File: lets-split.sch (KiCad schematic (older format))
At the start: 54 parts

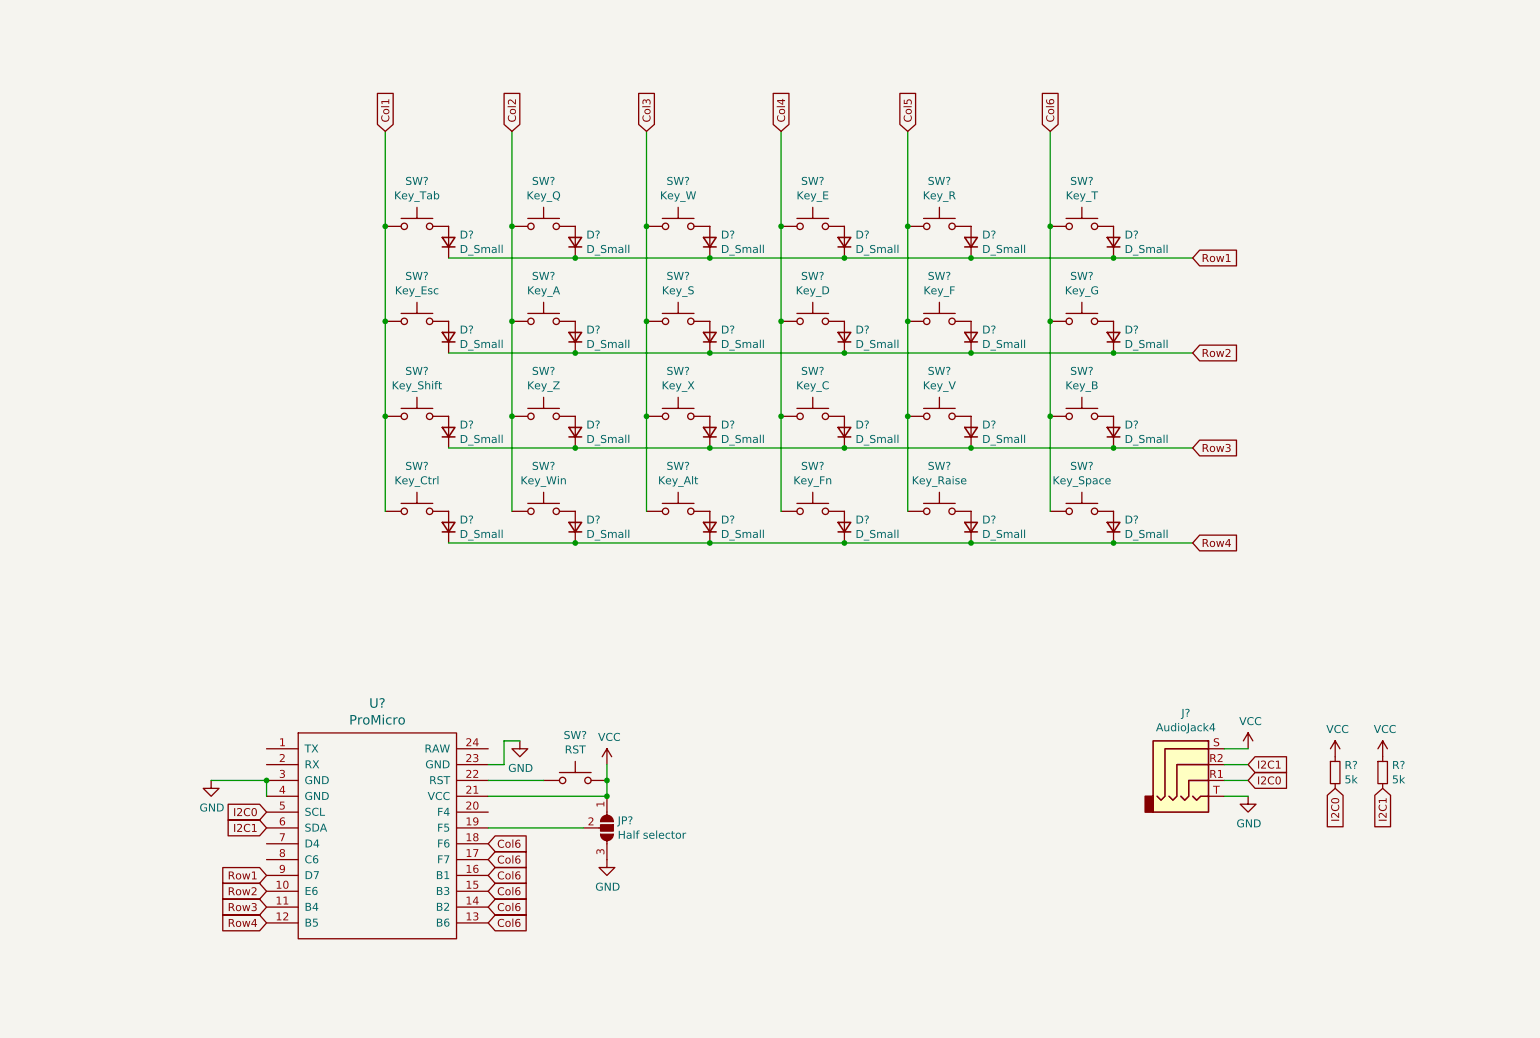
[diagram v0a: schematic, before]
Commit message: added annotations
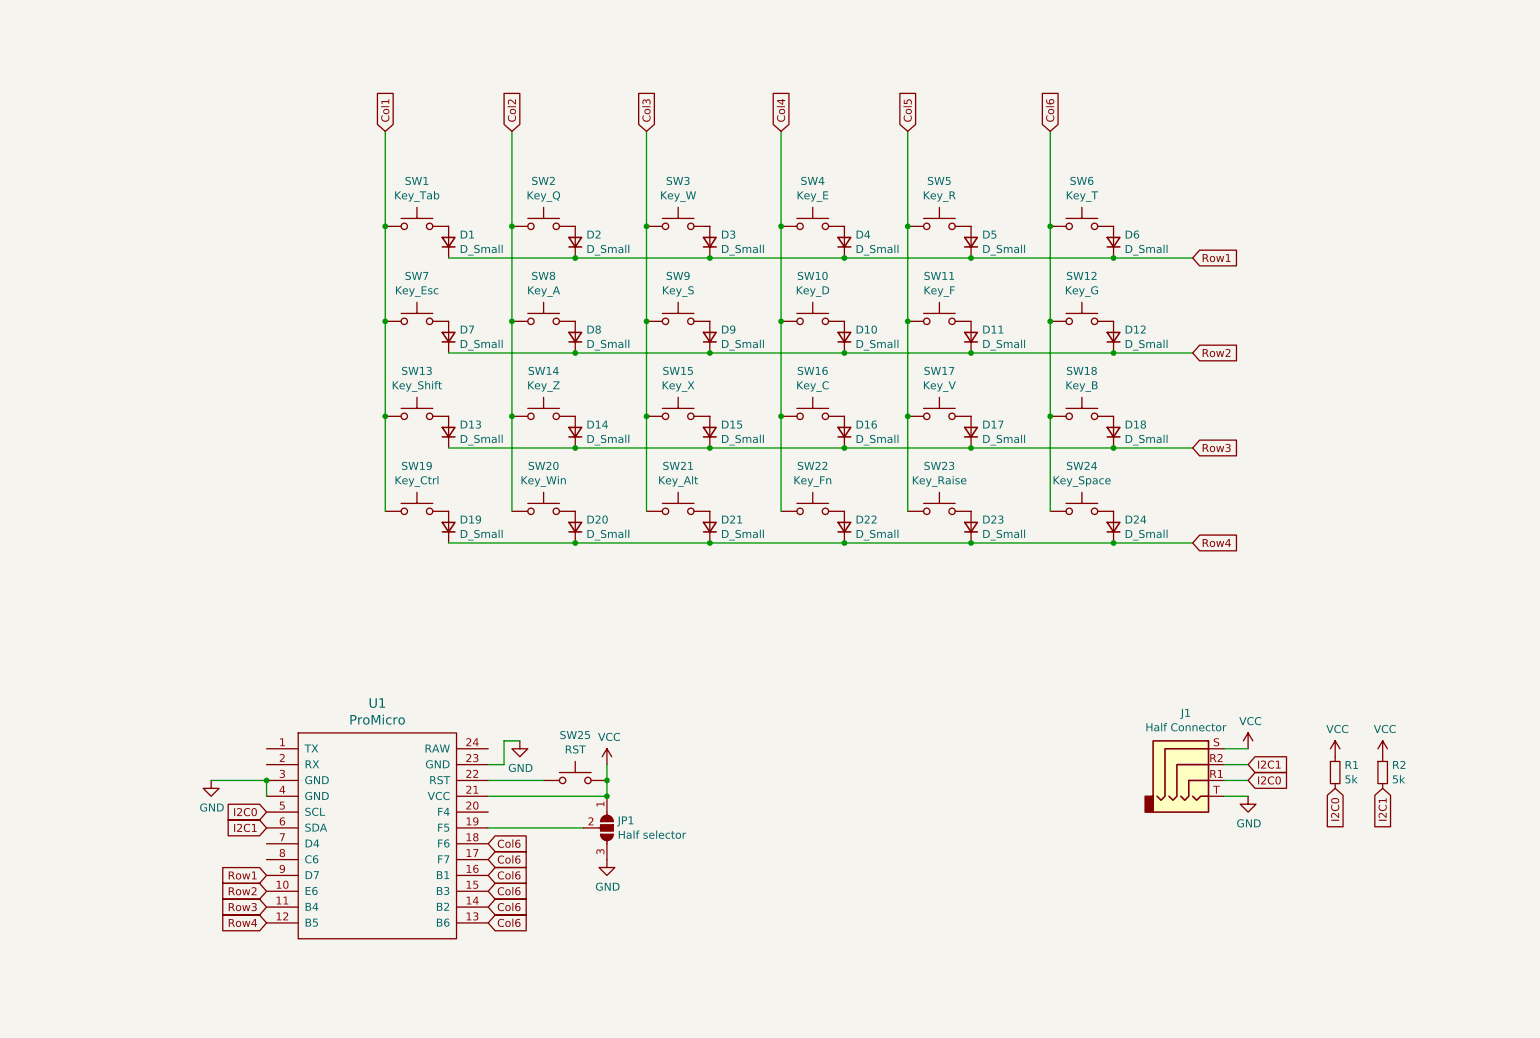
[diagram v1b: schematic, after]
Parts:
- J1: renamed from J?; value AudioJack4 -> Half Connector
- gave numbers to parts that had none: 53

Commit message: Assigned footprints to most components
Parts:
- D1, D10, D11, D12, D13, D14, D15, D16, D17, D18, D19, D2, D20, D21, D22, D23, D24, D3, D4, D5, D6, D7, D8, D9: footprint (none) -> Diode_THT:D_DO-34_SOD68_P7.62mm_Horizontal
- JP1: footprint (none) -> Jumper:SolderJumper-3_P1.3mm_Open_RoundedPad1.0x1.5mm
- R1, R2: footprint (none) -> Resistor_THT:R_Axial_DIN0207_L6.3mm_D2.5mm_P10.16mm_Horizontal
- SW1, SW10, SW11, SW12, SW13, SW14, SW15, SW16, SW17, SW18, SW19, SW2, SW20, SW21, SW22, SW23, SW24, SW3, SW4, SW5, SW6, SW7, SW8, SW9: footprint (none) -> keyswitches:SW_MX_reversible
- SW25: footprint (none) -> Button_Switch_THT:SW_PUSH_6mm
- U1: footprint (none) -> promicro:ProMicro

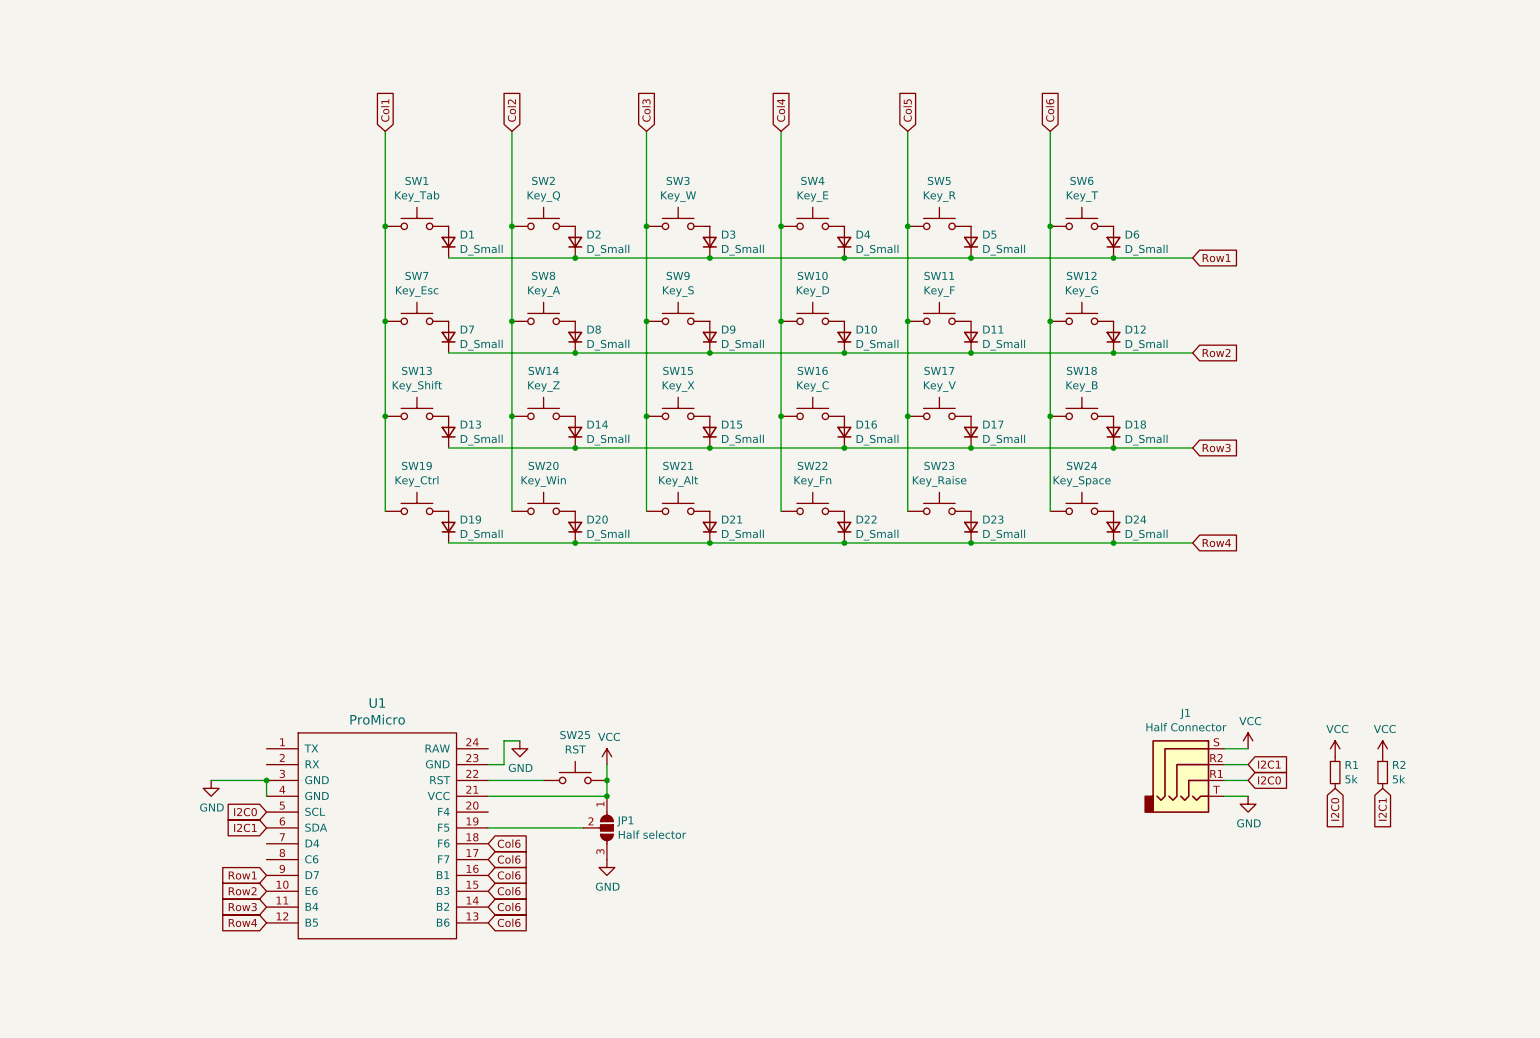
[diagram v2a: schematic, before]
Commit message: Switched TRRS to USB-C abuse. Should be safer.
Also added resistor on data pins
And replaced hand selector jumper with a pull up/down resistor (lower
power I guess?)
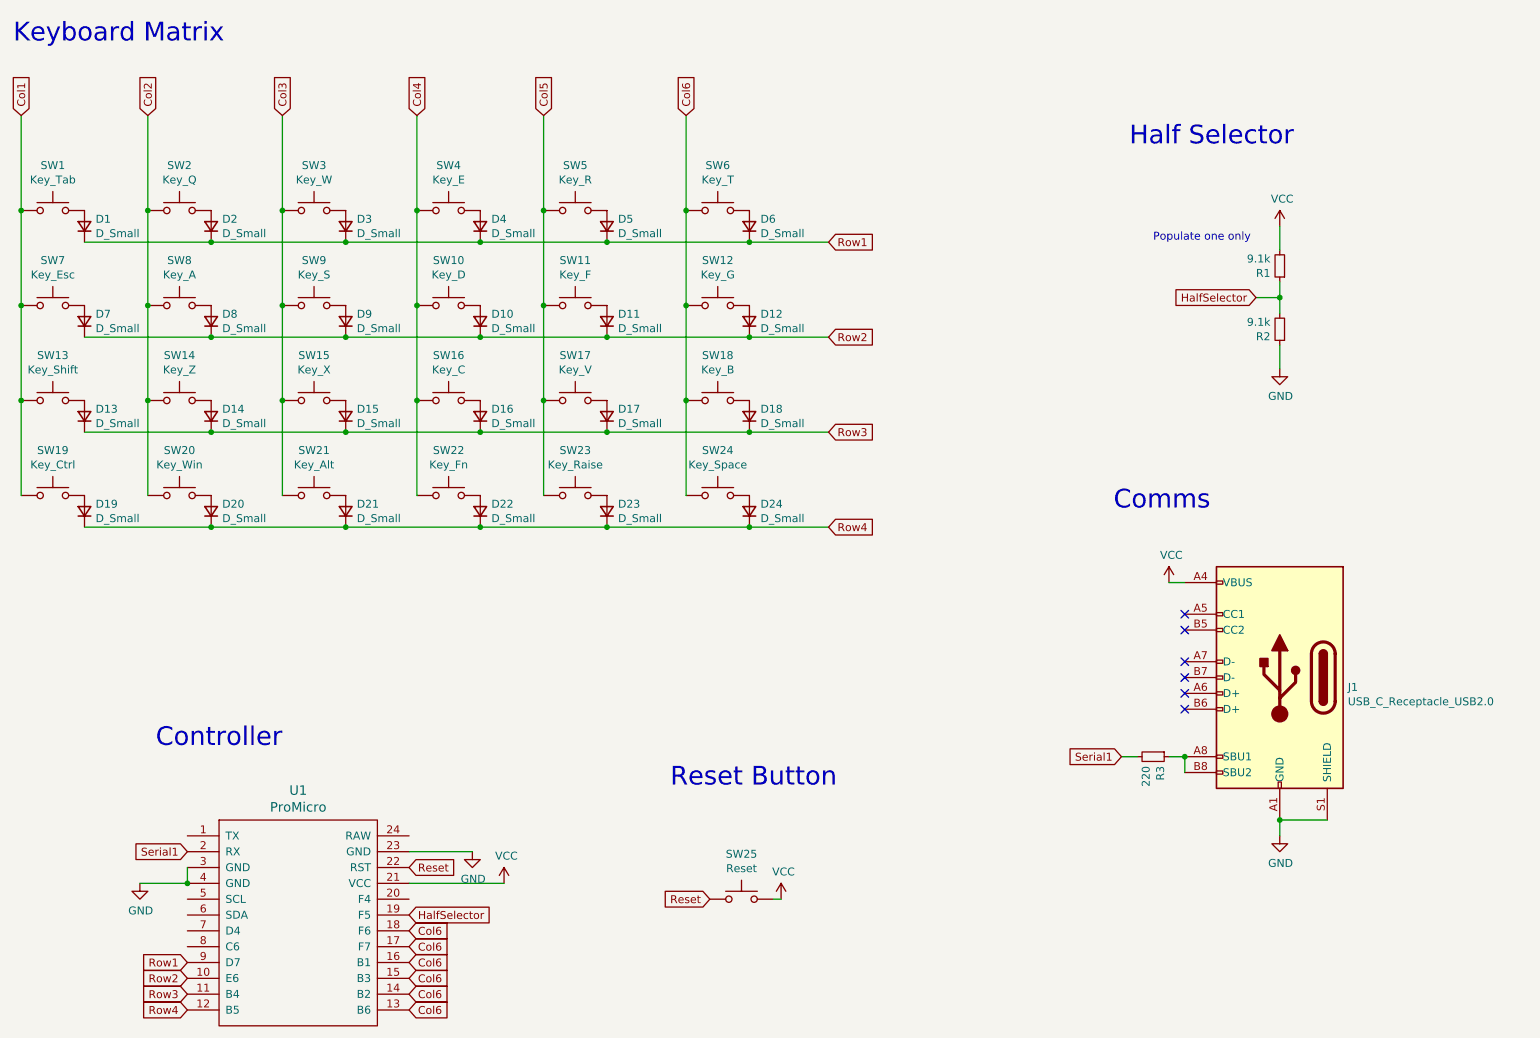
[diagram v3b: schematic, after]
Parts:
- removed J1: Half Connector, symbol Connector:AudioJack4
- removed JP1: Half selector, Jumper:SolderJumper-3_P1.3mm_Open_RoundedPad1.0x1.5mm, symbol Jumper:SolderJumper_3_Open
- added J1: USB_C_Receptacle_USB2.0, Connector_USB:USB_C_Receptacle_GCT_USB4085, symbol Connector:USB_C_Receptacle_USB2.0
- added R3: 220, Resistor_THT:R_Axial_DIN0207_L6.3mm_D2.5mm_P10.16mm_Horizontal, symbol Device:R_Small
- R1, R2: value 5k -> 9.1k
- SW25: value RST -> Reset; footprint Button_Switch_THT:SW_PUSH_6mm -> keyswitches:SW_MX_reversible
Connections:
- net GND: now also R2.1, J1.A1 (GND), J1.A12 (GND), J1.B1 (GND), J1.B12 (GND), J1.S1 (SHIELD)
- net VCC: now also R1.2, J1.A4 (VBUS), J1.A9 (VBUS), J1.B4 (VBUS), J1.B9 (VBUS); no longer R1.1, R2.1
- net HalfSelector: now reaches U1.19 (F5)
- net HalfSelector: now also R1.1, R2.2
- net Serial1: now reaches U1.2 (RX)
- net Serial1: now also R3.2
- net Reset: now reaches SW25.1, U1.22 (RST)
- net I2C0: no longer names the net of U1.5 (SCL)
- net I2C0: no longer R1.2
- net I2C1: no longer names the net of U1.6 (SDA)
- net I2C1: no longer R2.2
- new net: J1.A8 (SBU1), J1.B8 (SBU2), R3.1
- no-connect marks 0 -> 6
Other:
- note added: "Comms"
- note added: "Controller"
- note added: "Half Selector"
- note added: "Keyboard Matrix"
- note added: "Populate one only"
- note added: "Reset Button"
- moved on the sheet: D1, D10, D11, D12, D13, D14, D15, D16, D17, D18, D19, D2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
